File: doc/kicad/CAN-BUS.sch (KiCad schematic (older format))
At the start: 17 parts, among them K1 HFD2_005-S-L2-D, U1 PCF8574, U2 PCF8574, U3 PCF8574, U4 ULN2803A, U5 ULN2803A, U6 ULN2803A, U7 ULN2803A, U8 ULN2803A

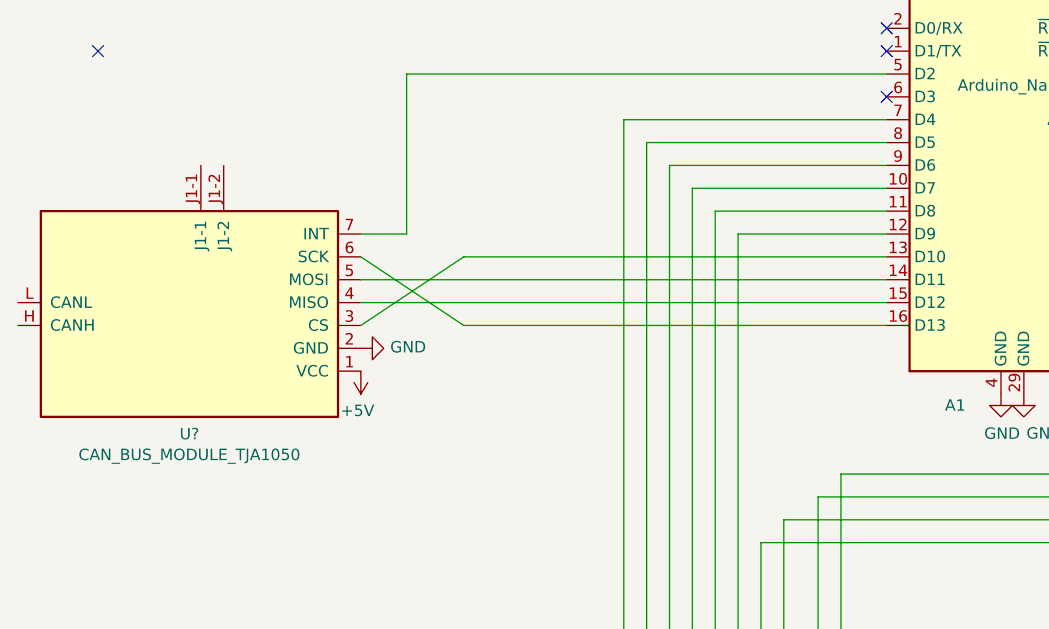
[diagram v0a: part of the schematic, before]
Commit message: Schaltplan angepasst
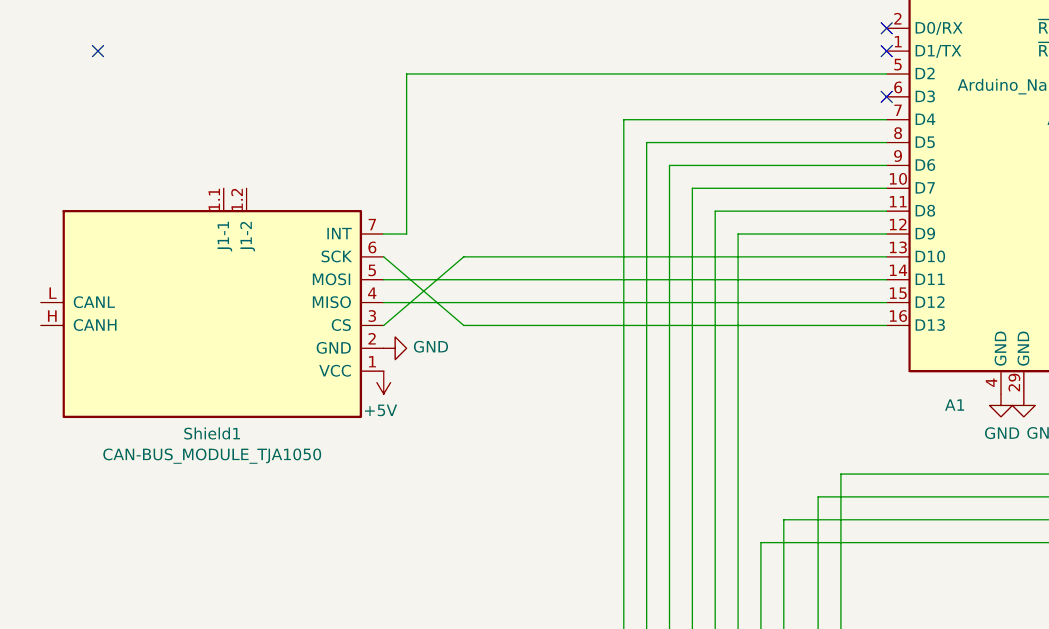
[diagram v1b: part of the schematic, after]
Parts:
- removed U?: CAN_BUS_MODULE_TJA1050, symbol CAN_BUS_MODULE_TJA1050_COPY:CAN_BUS_MODULE_TJA1050
- added Shield1: CAN-BUS_MODULE_TJA1050, kicad-lib:MCP2515_CAN_MODULE_BY0-10, symbol CAN-BUS-MODULE-TJA1050:CAN-BUS_MODULE_TJA1050
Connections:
- net +5V: now also Shield1.1 (VCC)
- net GND: now also Shield1.2 (GND)
- net at A1.13 (D10): now also Shield1.3 (CS)
- net at A1.14 (D11): now also Shield1.5 (MOSI)
- net at A1.15 (D12): now also Shield1.4 (MISO)
- net at A1.16 (D13): now also Shield1.6 (SCK)
- net at A1.5 (D2): now also Shield1.7 (INT)
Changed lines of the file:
@@
 	5700 4600 5550 4600
 Wire Wire Line
-	2350 1950 2350 2650
+	2250 2750 2600 3050
 Wire Wire Line
-	2350 2650 2150 2650
-Wire Wire Line
-	2150 2750 2600 3050
-Wire Wire Line
-	2150 3050 2600 2750
-Wire Wire Line
-	2350 1950 4450 1950
+	2250 3050 2600 2750
 Wire Wire Line
 	2600 2750 4450 2750
@@
 	2600 3050 4450 3050
 Wire Wire Line
-	2150 2950 4450 2950
+	2250 2950 4450 2950
 Wire Wire Line
-	2150 2850 4450 2850
+	2250 2850 4450 2850
 $Comp
-L power:+5V #PWR?
+L power:+5V #PWR0124
 U 1 1 6060A93E
-P 2150 3250
-F 0 "#PWR?" H 2150 3100 50  0001 C CNN
-F 1 "+5V" H 2165 3423 50  0000 C CNN
-F 2 "" H 2150 3250 50  0001 C CNN
-F 3 "" H 2150 3250 50  0001 C CNN
-	1    2150 3250
+P 2250 3250
+F 0 "#PWR0124" H 2250 3100 50  0001 C CNN
+F 1 "+5V" H 2265 3423 50  0000 C CNN
+F 2 "" H 2250 3250 50  0001 C CNN
+F 3 "" H 2250 3250 50  0001 C CNN
+	1    2250 3250
 	-1   0    0    1
 $EndComp
 $Comp
-L CAN_BUS_MODULE_TJA1050_COPY:CAN_BUS_MODULE_TJA1050 U?
-U 1 1 60580973
-P 1450 2850
-F 0 "U?" H 1400 2175 50  0000 C CNN
-F 1 "CAN_BUS_MODULE_TJA1050" H 1400 2084 50  0000 C CNN
-F 2 "" H 1450 2850 50  0001 C CNN
-F 3 "" H 1450 2850 50  0001 C CNN
-	1    1450 2850
+L power:GND #PWR0125
+U 1 1 6058B6A1
+P 2250 3150
+F 0 "#PWR0125" H 2250 2900 50  0001 C CNN
+F 1 "GND" V 2255 3022 50  0000 R CNN
+F 2 "" H 2250 3150 50  0001 C CNN
+F 3 "" H 2250 3150 50  0001 C CNN
+	1    2250 3150
+	0    -1   -1   0
+$EndComp
+$Comp
+L CAN-BUS-MODULE-TJA1050:CAN-BUS_MODULE_TJA1050 Shield1
+U 1 1 60585225
+P 1550 2850
+F 0 "Shield1" H 1500 2175 50  0000 C CNN
+F 1 "CAN-BUS_MODULE_TJA1050" H 1500 2084 50  0000 C CNN
+F 2 "kicad-lib:MCP2515_CAN_MODULE_BY0-10" H 1550 2850 50  0001 C CIN
+F 3 "" H 1550 2850 50  0001 C CNN
+	1    1550 2850
 	1    0    0    -1
 $EndComp
-$Comp
-L power:GND #PWR?
-U 1 1 6058B6A1
-P 2150 3150
-F 0 "#PWR?" H 2150 2900 50  0001 C CNN
-F 1 "GND" V 2155 3022 50  0000 R CNN
-F 2 "" H 2150 3150 50  0001 C CNN
-F 3 "" H 2150 3150 50  0001 C CNN
-	1    2150 3150
-	0    -1   -1   0
-$EndComp
+Wire Wire Line
+	2350 1950 4450 1950
+Wire Wire Line
+	2350 1950 2350 2650
+Wire Wire Line
+	2250 2650 2350 2650
 $EndSCHEMATC

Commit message: initial
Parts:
- added C1, C2, C3: 100n, Capacitors_THT:C_Disc_D7.0mm_W2.5mm_P5.00mm, symbol Device:C
- added J1: RJ45_LED_Shielded, Connectors:RJ45_TRANSFO, symbol Connector:RJ45_LED_Shielded
- added J10, J11, J12, J13: Conn_01x06_Female, symbol Connector:Conn_01x06_Female
- added J2: RJ45_Shielded, Connectors:RJ45_8, symbol Connector:RJ45_Shielded
- added J3: Power, symbol Connector:Conn_01x02_Female
- added J4: Weiche 1, symbol Connector:Conn_01x03_Female
- added J5: Weiche 2, symbol Connector:Conn_01x03_Female
- added J6: Weiche 3, symbol Connector:Conn_01x03_Female
- added J7: Weiche 4, symbol Connector:Conn_01x03_Female
- added J8: Weiche 5, symbol Connector:Conn_01x03_Female
- added J9: Power Weiche, symbol Connector:Conn_01x02_Female
- added JP1: Jumper, symbol Device:Jumper
- added R4, R5: 4k7, Resistors_SMD:R_0603, symbol Device:R
- added R6: 1K, Resistors_SMD:R_0603, symbol Device:R
- renumbered JP3 to JP2, JP1 to JP3, JP2 to JP4, R3 to R1, R1 to R3, U7 to U1, U8 to U2, U1 to U3, U2 to U4, U3 to U5, U4 to U6, U5 to U7, U6 to U8
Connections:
- net +5V: now also C1.1, C2.1, C3.1, J1.8, J10.1 (Pin_1), J11.1 (Pin_1), J12.1 (Pin_1), J13.1 (Pin_1), J2.8, J3.1 (Pin_1), R4.2, R5.2, R6.2
- net GND: now also U2.9 (GND), C1.2, C2.2, C3.2, J1.3, J1.7, J1.9, J2.3, J2.7, J3.2 (Pin_2), J9.2 (Pin_2)
- net at A1.10 (D7): now also U1.5 (I5); no longer U1.4 (I4)
- net at A1.11 (D8): now also U1.4 (I4); no longer U1.5 (I5)
- net at A1.12 (D9): now also U1.3 (I3); no longer U1.6 (I6)
- net at A1.19 (A0): now also U1.1 (I1); no longer U1.7 (I7)
- net at A1.20 (A1): now also U1.2 (I2); no longer U1.8 (I8)
- net at A1.23 (A4), U3.15 (SDA), U4.15 (SDA)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: now also R5.1
- net at A1.24 (A5), U3.14 (SCL), U4.14 (SCL)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: now also R4.1
- net at A1.7 (D4): now also U1.8 (I8); no longer U1.1 (I1)
- net at A1.8 (D5): now also U1.7 (I7); no longer U1.2 (I2)
- net at A1.9 (D6): now also U1.6 (I6); no longer U1.3 (I3)
- net at U6.11 (O8): now also J12.4 (Pin_4)
- net at U6.12 (O7): now also J12.3 (Pin_3)
- net at U6.13 (O6): now also J12.2 (Pin_2)
- net at U6.14 (O5): now also J11.6 (Pin_6)
- net at U6.15 (O4): now also J11.5 (Pin_5)
- net at U6.16 (O3): now also J11.4 (Pin_4)
- net at U6.17 (O2): now also J11.3 (Pin_3)
- net at U6.18 (O1): now also J11.2 (Pin_2)
- net at U7.11 (O8): now also J10.2 (Pin_2)
- net at U7.12 (O7): now also J13.6 (Pin_6)
- net at U7.13 (O6): now also J13.5 (Pin_5)
- net at U7.14 (O5): now also J13.4 (Pin_4)
- net at U7.15 (O4): now also J13.3 (Pin_3)
- net at U7.16 (O3): now also J13.2 (Pin_2)
- net at U7.17 (O2): now also J12.6 (Pin_6)
- net at U7.18 (O1): now also J12.5 (Pin_5)
- net at U8.15 (O4): now also J10.6 (Pin_6)
- net at U8.16 (O3): now also J10.5 (Pin_5)
- net at U8.17 (O2): now also J10.4 (Pin_4)
- net at U8.18 (O1): now also J10.3 (Pin_3)
- net at Shield1.H (CANH): now also J1.1, J2.1
- net at Shield1.L (CANL): now also J1.2, J2.2
- net at U1.10 (COM): now also JP1.1
- net at U1.11 (O8): now also J7.3 (Pin_3)
- net at U1.12 (O7): now also J7.2 (Pin_2)
- net at U1.13 (O6): now also J6.3 (Pin_3)
- net at U1.14 (O5): now also J6.2 (Pin_2)
- net at U1.15 (O4): now also J5.3 (Pin_3)
- net at U1.16 (O3): now also J5.2 (Pin_2)
- net at U1.17 (O2): now also J4.3 (Pin_3)
- net at U1.18 (O1): now also J4.2 (Pin_2)
- net +12V: now reaches U2.10 (COM)
- net +12V: now also J4.1 (Pin_1), J5.1 (Pin_1), J6.1 (Pin_1), J7.1 (Pin_1), J8.1 (Pin_1), J9.1 (Pin_1), JP1.2
- net at U2.17 (O2): now also J8.3 (Pin_3)
- net at U2.18 (O1): now also J8.2 (Pin_2)
- new net: J1.10, R6.1
- new net: J1.4, J2.4
- new net: J1.5, J2.5
- new net: J1.6, J2.6
- no-connect marks 13 -> 12
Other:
- moved on the sheet: JP2, JP3, JP4, K1, R1, R2, R3, Shield1, U1, U2
